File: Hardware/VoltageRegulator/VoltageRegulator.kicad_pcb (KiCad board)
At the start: 2 copper layers, 22.9 x 19 mm, 9 parts, among them J1 Conn_01x04, U1 TPS7A2501DRVR

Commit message: Layout changes plus 3D model
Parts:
- moved R3 6.73 mm to (142.6, 100.3), turned to 0 degrees
- moved C1 1.91 mm to (139.1, 94.5)
- moved C2 1.91 mm to (139.1, 102.4)
- moved R2 0.38 mm to (142.6, 101.9)
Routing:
- net Net-(U1-FB): track 14.6 -> 2.93 mm
- net VCC: track 16.6 -> 15.1 mm
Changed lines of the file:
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@@
   (net 5 "Net-(U1-FB)")
   (footprint "Capacitor_SMD:C_0805_2012Metric" (layer "F.Cu")
-    (at 137.16 94.488 -90)
+    (at 139.065 94.488 -90)
     (descr "Capacitor SMD 0805 (2012 Metric), square (rectangular) end terminal, IPC_7351 nominal, (Body size source: IPC-SM-782 page 76, https://www.pcb-3d.com/wordpress/wp-content/uploads/ipc-sm-782a_amendment_1_and_2.pdf, https://docs.google.com/spreadsheets/d/1BsfQQcO9C6DZCsRaXUlFlo91Tg2WpOkGARC1WS5S8t0/edit?usp=sharing), generated with kicad-footprint-generator")
     (tags "capacitor")
@@
     (property "ki_keywords" "cap capacitor")
     (attr smd)
-    (fp_text reference "C1" (at 0 1.905 90) (layer "F.SilkS")
-        (effects (font (size 1 1) (thickness 0.15)))
-    )
-    (fp_text value "1u" (at -2.225 1.905 90) (layer "F.Fab")
+    (fp_text reference "C1" (at -2.286 -0.127 -180) (layer "F.SilkS")
+        (effects (font (size 1 1) (thickness 0.15)))
+    )
+    (fp_text value "1u" (at -3.683 0 -180) (layer "F.Fab")
         (effects (font (size 1 1) (thickness 0.15)))
     )
@@
   )
   (footprint "Resistor_SMD:R_0603_1608Metric" (layer "F.Cu")
-    (at 142.558 101.473 180)
+    (at 142.558 101.854 180)
     (descr "Resistor SMD 0603 (1608 Metric), square (rectangular) end terminal, IPC_7351 nominal, (Body size source: IPC-SM-782 page 72, https://www.pcb-3d.com/wordpress/wp-content/uploads/ipc-sm-782a_amendment_1_and_2.pdf), generated with kicad-footprint-generator")
     (tags "resistor")
@@
   )
   (footprint "Capacitor_SMD:C_0805_2012Metric" (layer "F.Cu")
-    (at 137.16 102.362 90)
+    (at 139.065 102.362 90)
     (descr "Capacitor SMD 0805 (2012 Metric), square (rectangular) end terminal, IPC_7351 nominal, (Body size source: IPC-SM-782 page 76, https://www.pcb-3d.com/wordpress/wp-content/uploads/ipc-sm-782a_amendment_1_and_2.pdf, https://docs.google.com/spreadsheets/d/1BsfQQcO9C6DZCsRaXUlFlo91Tg2WpOkGARC1WS5S8t0/edit?usp=sharing), generated with kicad-footprint-generator")
     (tags "capacitor")
@@
     (property "ki_keywords" "cap capacitor")
     (attr smd)
-    (fp_text reference "C2" (at 0 -1.905 90) (layer "F.SilkS")
-        (effects (font (size 1 1) (thickness 0.15)))
-    )
-    (fp_text value "2.2u" (at -2.86 -1.905 90) (layer "F.Fab")
+    (fp_text reference "C2" (at -2.413 0 180) (layer "F.SilkS")
+        (effects (font (size 1 1) (thickness 0.15)))
+    )
+    (fp_text value "2.2u" (at -3.683 0 180) (layer "F.Fab")
         (effects (font (size 1 1) (thickness 0.15)))
     )
@@
   )
   (footprint "Resistor_SMD:R_0603_1608Metric" (layer "F.Cu")
-    (at 142.557 93.599 180)
+    (at 142.557 100.33)
     (descr "Resistor SMD 0603 (1608 Metric), square (rectangular) end terminal, IPC_7351 nominal, (Body size source: IPC-SM-782 page 72, https://www.pcb-3d.com/wordpress/wp-content/uploads/ipc-sm-782a_amendment_1_and_2.pdf), generated with kicad-footprint-generator")
     (tags "resistor")
@@
     (property "ki_keywords" "R res resistor")
     (attr smd)
-    (fp_text reference "R3" (at -2.731 0) (layer "F.SilkS")
-        (effects (font (size 1 1) (thickness 0.15)))
-    )
-    (fp_text value "1M" (at -5.017 0) (layer "F.Fab")
+    (fp_text reference "R3" (at 2.731 0) (layer "F.SilkS")
+        (effects (font (size 1 1) (thickness 0.15)))
+    )
+    (fp_text value "1M" (at 4.763 0) (layer "F.Fab")
         (effects (font (size 1 1) (thickness 0.15)))
     )
@@
     (fp_line (start 0.8 0.4125) (end -0.8 0.4125)
       (stroke (width 0.1) (type solid)) (layer "F.Fab"))
-    (pad "1" smd roundrect (at -0.825 0 180) (size 0.8 0.95) (layers "F.Cu" "F.Paste" "F.Mask") (roundrect_rratio 0.25)
+    (pad "1" smd roundrect (at -0.825 0) (size 0.8 0.95) (layers "F.Cu" "F.Paste" "F.Mask") (roundrect_rratio 0.25)
       (net 5 "Net-(U1-FB)") (pintype "passive"))
-    (pad "2" smd roundrect (at 0.825 0 180) (size 0.8 0.95) (layers "F.Cu" "F.Paste" "F.Mask") (roundrect_rratio 0.25)
+    (pad "2" smd roundrect (at 0.825 0) (size 0.8 0.95) (layers "F.Cu" "F.Paste" "F.Mask") (roundrect_rratio 0.25)
       (net 2 "GND") (pintype "passive"))
     (model "${KICAD6_3DMODEL_DIR}/Resistor_SMD.3dshapes/R_0603_1608Metric.wrl"
@@
     (pad "9" thru_hole circle (at 0 -0.549999 90) (size 0.499999 0.499999) (drill 0.2032) (layers "*.Cu" "*.Mask")
       (net 2 "GND") (zone_connect 2))
+    (model "${KIPRJMOD}/Libraries/TPS7A2501DRVR.pretty/DRV0006A.stp"
+      (offset (xyz 0 0 0))
+      (scale (xyz 1 1 1))
+      (rotate (xyz 0 0 0))
+    )
   )
   (footprint "MountingHole:MountingHole_3.2mm_M3" (layer "F.Cu")
@@
   (segment (start 141.716999 97.473968) (end 143.318032 97.473968) (width 1.016) (layer "F.Cu") (net 2))
   (segment (start 141.716999 96.395936) (end 141.716999 97.473968) (width 0.25) (layer "F.Cu") (net 2))
-  (segment (start 135.062 103.312) (end 137.16 103.312) (width 0.381) (layer "F.Cu") (net 3))
-  (segment (start 141.066998 98.452) (end 141.066998 99.405002) (width 0.381) (layer "F.Cu") (net 3))
-  (segment (start 137.226 103.378) (end 137.16 103.312) (width 0.381) (layer "F.Cu") (net 3))
-  (segment (start 133.995 102.245) (end 135.062 103.312) (width 0.381) (layer "F.Cu") (net 3))
-  (segment (start 141.066998 99.405002) (end 137.16 103.312) (width 0.381) (layer "F.Cu") (net 3))
+  (segment (start 140.97 98.545965) (end 140.97 103.378) (width 0.381) (layer "F.Cu") (net 3))
   (segment (start 132.08 102.245) (end 133.995 102.245) (width 0.381) (layer "F.Cu") (net 3))
-  (segment (start 141.733 103.378) (end 137.226 103.378) (width 0.381) (layer "F.Cu") (net 3))
+  (segment (start 141.066998 98.448967) (end 140.97 98.545965) (width 0.381) (layer "F.Cu") (net 3))
+  (segment (start 133.995 102.245) (end 135.128 103.378) (width 0.381) (layer "F.Cu") (net 3))
+  (segment (start 135.128 103.378) (end 140.97 103.378) (width 0.381) (layer "F.Cu") (net 3))
+  (segment (start 140.97 103.378) (end 141.733 103.378) (width 0.381) (layer "F.Cu") (net 3))
   (segment (start 143.383 103.378) (end 143.383 101.473) (width 0.25) (layer "F.Cu") (net 4))
-  (segment (start 144.437 100.673) (end 142.533 100.673) (width 0.25) (layer "F.Cu") (net 5))
   (segment (start 141.733 101.473) (end 141.716999 101.456999) (width 0.25) (layer "F.Cu") (net 5))
-  (segment (start 143.382 93.599) (end 144.399 93.599) (width 0.25) (layer "F.Cu") (net 5))
-  (segment (start 142.533 100.673) (end 141.733 101.473) (width 0.25) (layer "F.Cu") (net 5))
   (segment (start 141.716999 101.456999) (end 141.716999 98.552) (width 0.25) (layer "F.Cu") (net 5))
-  (segment (start 145.034 100.076) (end 144.437 100.673) (width 0.25) (layer "F.Cu") (net 5))
-  (segment (start 144.399 93.599) (end 145.034 94.234) (width 0.25) (layer "F.Cu") (net 5))
-  (segment (start 145.034 94.234) (end 145.034 100.076) (width 0.25) (layer "F.Cu") (net 5))
   (zone (net 2) (net_name "GND") (layer "F.Cu") (hatch edge 0.5)
     (connect_pads (clearance 0.5))

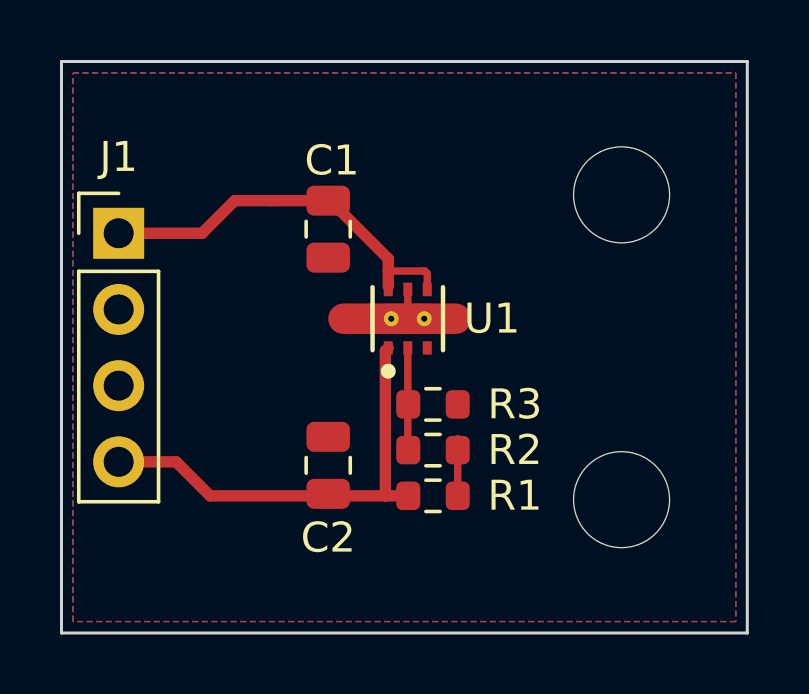
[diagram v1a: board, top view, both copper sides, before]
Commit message: Smaller board with isolated mounting holes
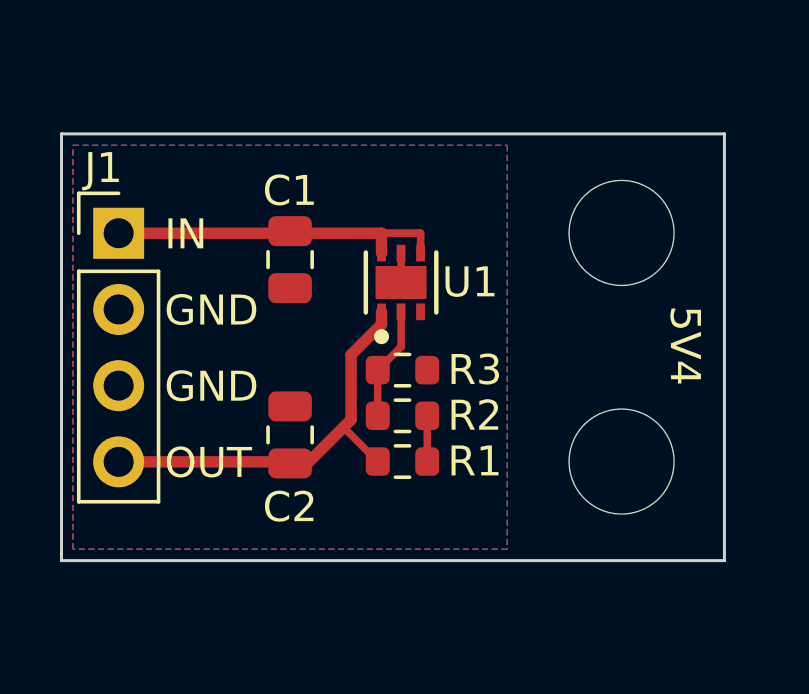
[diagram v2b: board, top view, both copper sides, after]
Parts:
- added G***: LOGO, Clough42Logo:Clough42Logo, B.Cu at (140.0, 98.7)
- H1, H2: footprint MountingHole:MountingHole_3.2mm_M3 -> MountingHole:MountingHole_3.5mm
- U1: footprint TPS7A2501:DRV0006A-MFG -> TPS7A2501:DRV0006A-IPC_C
- moved C1 1.63 mm to (137.8, 95.5)
- moved C2 1.63 mm to (137.8, 101.3)
- moved R1 1.53 mm to (141.5, 102.2)
- moved R2 1.53 mm to (141.5, 100.7)
- moved R3 1.53 mm to (141.5, 99.2)
- moved H1 1.27 mm to (148.8, 94.6)
- moved H2 1.27 mm to (148.8, 102.2)
- moved U1 1.23 mm to (141.5, 96.3)
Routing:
- net GND: track 4.82 -> 0.98 mm
- net VCC: track 15.1 -> 14.0 mm
- net +BATT: track 13.0 -> 12.1 mm
- net Net-(U1-FB): track 2.93 -> 3.79 mm
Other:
- board size 22.9 x 19 mm -> 22.1 x 14.2 mm
- board text added: "5V4"
- board text added: "5V4 Regulator 2023 v1.0"
- board text added: "GND"
- board text added: "IN"
- board text added: "OUT"
